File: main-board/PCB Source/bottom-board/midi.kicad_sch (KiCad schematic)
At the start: 14 parts, among them P6 AudioJack3, P7 AudioJack3, Q12 2N7002, Q13 2N7002, U11 6N137S

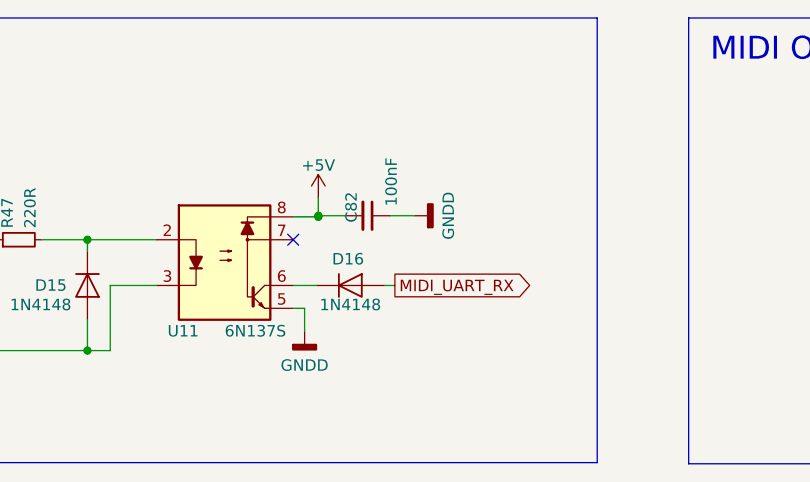
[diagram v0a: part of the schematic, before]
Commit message: mainboard: add bias buffer, update MPNs, clean schematic
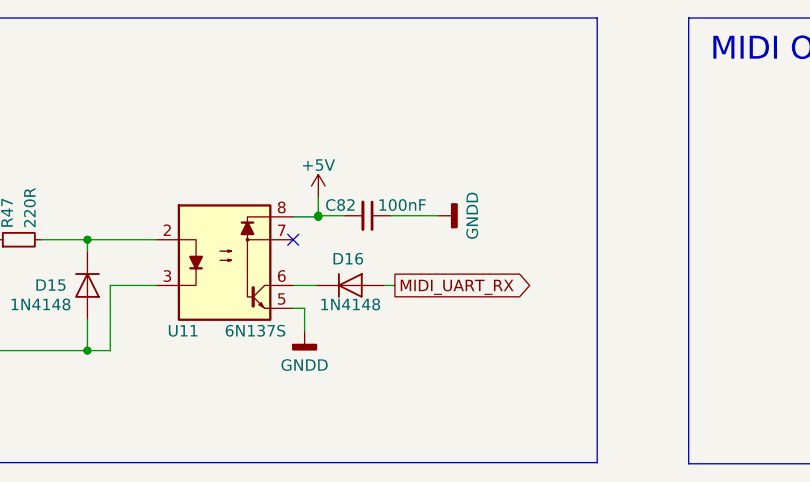
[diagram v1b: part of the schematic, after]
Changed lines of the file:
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@@
     (title "MOD Dwarf - Main Board")
     (date "2021-09-06")
-    (rev "1.3")
+    (rev "3.0")
     (company "MOD Devices GmbH")
     (comment 1 "Dwarf Audio processing board")
@@
     (stroke (width 0) (type default) (color 0 0 0 0))
   )
-  (wire (pts (xy 118.11 91.821) (xy 115.443 91.821))
+  (wire (pts (xy 115.443 91.821) (xy 120.777 91.821))
     (stroke (width 0) (type default) (color 0 0 0 0))
   )
@@
   (symbol (lib_id "bottom-board-rescue:C_Small") (at 112.903 91.821 270) (unit 1)
     (in_bom yes) (on_board yes)
-    (property "Reference" "C82" (id 0) (at 111.125 89.154 0)
-      (effects (font (size 1.27 1.27)) (justify left))
-    )
-    (property "Value" "100nF" (id 1) (at 115.57 85.344 0)
+    (property "Reference" "C82" (id 0) (at 108.204 90.678 90)
+      (effects (font (size 1.27 1.27)) (justify left))
+    )
+    (property "Value" "100nF" (id 1) (at 114.046 90.678 90)
       (effects (font (size 1.27 1.27)) (justify left))
     )
@@
     (pin "2")
   )
-  (symbol (lib_id "bottom-board-rescue:GNDD-power") (at 118.11 91.821 90) (unit 1)
-    (in_bom yes) (on_board yes)
-    (property "Reference" "#PWR0264" (id 0) (at 124.46 91.821 0)
-      (effects (font (size 1.27 1.27)) hide)
-    )
-    (property "Value" "GNDD" (id 1) (at 121.92 91.821 0))
-    (property "Footprint" "" (id 2) (at 118.11 91.821 0)
-      (effects (font (size 1.524 1.524)))
-    )
-    (property "Datasheet" "" (id 3) (at 118.11 91.821 0)
-      (effects (font (size 1.524 1.524)))
-    )
+  (symbol (lib_id "bottom-board-rescue:GNDD-power") (at 120.777 91.821 90) (unit 1)
+    (in_bom yes) (on_board yes)
+    (property "Reference" "#PWR0264" (id 0) (at 127.127 91.821 0)
+      (effects (font (size 1.27 1.27)) hide)
+    )
+    (property "Value" "GNDD" (id 1) (at 124.587 91.821 0))
+    (property "Footprint" "" (id 2) (at 120.777 91.821 0)
+      (effects (font (size 1.524 1.524)))
+    )
+    (property "Datasheet" "" (id 3) (at 120.777 91.821 0)
+      (effects (font (size 1.524 1.524)))
+    )

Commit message: icnrease diode footprint, add extra input cap option
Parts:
- D15, D16: footprint Diode_SMD:D_SOD-323 -> Diode_SMD:D_SOD-323_HandSoldering
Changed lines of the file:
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@@
       (effects (font (size 1.27 1.27)) (justify right))
     )
-    (property "Footprint" "Diode_SMD:D_SOD-323" (id 2) (at 77.343 99.568 0)
+    (property "Footprint" "Diode_SMD:D_SOD-323_HandSoldering" (id 2) (at 77.343 99.568 0)
       (effects (font (size 1.27 1.27)) hide)
     )
@@
       (effects (font (size 1.27 1.27)) (justify right))
     )
-    (property "Footprint" "Diode_SMD:D_SOD-323" (id 2) (at 110.998 104.013 0)
+    (property "Footprint" "Diode_SMD:D_SOD-323_HandSoldering" (id 2) (at 110.998 104.013 0)
       (effects (font (size 1.27 1.27)) hide)
     )
